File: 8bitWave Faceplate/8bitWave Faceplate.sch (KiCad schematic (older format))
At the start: 45 parts, among them IC1 0.96_I2C_OLED, J1 I2C_VOL, J2 SPI, J3 EXTENSION, M1 Mounting, M2 Mounting, M3 Mounting, M4 Mounting, U1 74HC595_ALT, U2 74HC595_ALT

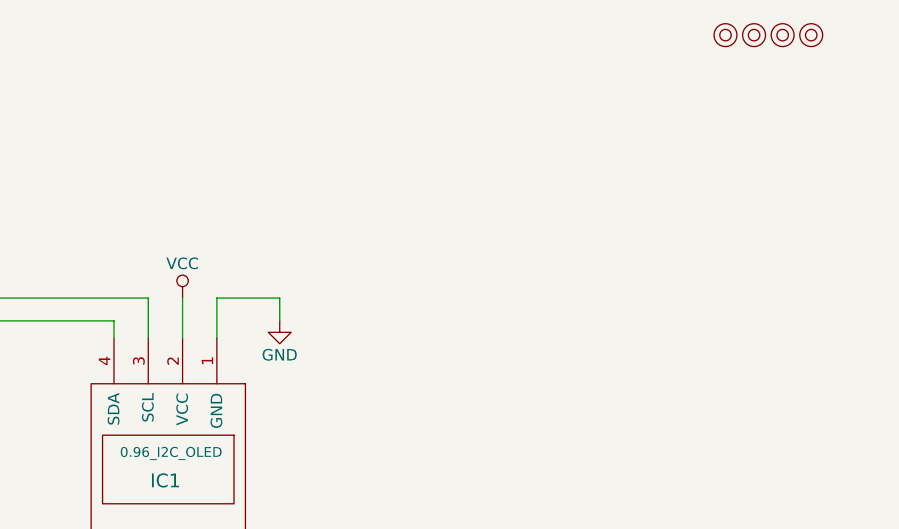
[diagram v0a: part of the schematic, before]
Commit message: Allow faceplate to choose OLED pin order
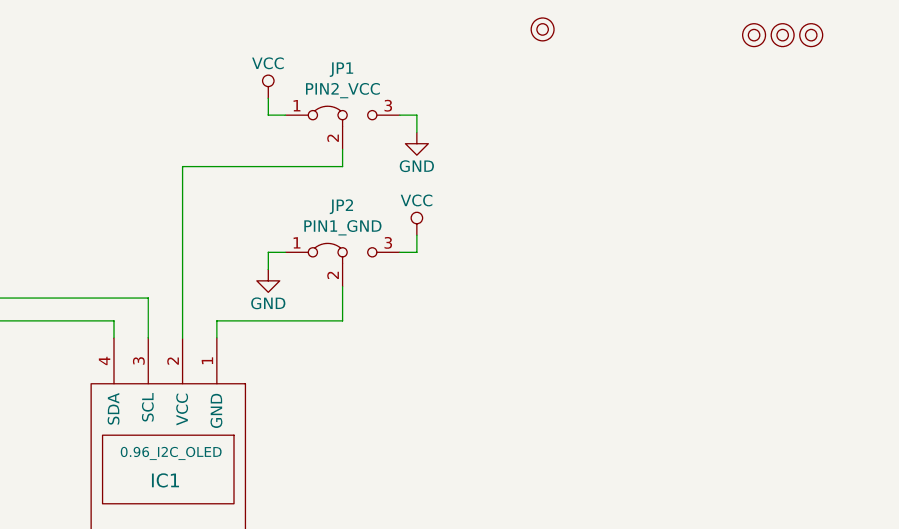
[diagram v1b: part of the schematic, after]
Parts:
- added JP1: PIN2_VCC, wire_pads:OLED_SEL, symbol Jumper:Jumper_3_Bridged12
- added JP2: PIN1_GND, wire_pads:OLED_SEL, symbol Jumper:Jumper_3_Bridged12
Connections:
- net GND: now also JP1.3 (B), JP2.1 (A); no longer IC1.1 (GND)
- net VCC: now also JP1.1 (A), JP2.3 (B); no longer IC1.2 (VCC)
- new net: IC1.1 (GND), JP2.2 (C)
- new net: IC1.2 (VCC), JP1.2 (C)
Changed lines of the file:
@@
 Title "8BIT WAVE Faceplate"
 Date ""
-Rev "A"
+Rev "B"
 Comp ""
 Comment1 ""
@@
 L mounting:Mounting M1
 U 1 1 5E3B603D
-P 10775 550
-F 0 "M1" H 10775 650 50  0001 C CNN
-F 1 "Mounting" H 10775 475 50  0001 C CNN
-F 2 "mounting:M3" H 10775 550 50  0001 C CNN
-F 3 "" H 10775 550 50  0001 C CNN
-	1    10775 550
+P 9975 525
+F 0 "M1" H 9975 625 50  0001 C CNN
+F 1 "Mounting" H 9975 450 50  0001 C CNN
+F 2 "mounting:M3" H 9975 525 50  0001 C CNN
+F 3 "" H 9975 525 50  0001 C CNN
+	1    9975 525
 	1    0    0    -1
 $EndComp
@@
 	7150 1900 7250 1800
 Wire Wire Line
-	8550 1700 8550 1875
-Wire Wire Line
 	8250 1700 7250 1700
 Wire Wire Line
@@
 Wire Wire Line
 	8100 1800 8100 1875
-Wire Wire Line
-	8550 1700 8825 1700
-Wire Wire Line
-	8825 1700 8825 1800
-$Comp
-L power:GND #PWR05
-U 1 1 5E3EF7B8
-P 8825 1800
-F 0 "#PWR05" H 8825 1550 50  0001 C CNN
-F 1 "GND" H 8825 1650 50  0000 C CNN
-F 2 "" H 8825 1800 50  0001 C CNN
-F 3 "" H 8825 1800 50  0001 C CNN
-	1    8825 1800
-	-1   0    0    -1
-$EndComp
-$Comp
-L power:VCC #PWR06
-U 1 1 5E3EF86D
-P 8400 1700
-F 0 "#PWR06" H 8400 1550 50  0001 C CNN
-F 1 "VCC" H 8400 1850 50  0000 C CNN
-F 2 "" H 8400 1700 50  0001 C CNN
-F 3 "" H 8400 1700 50  0001 C CNN
-	1    8400 1700
-	-1   0    0    -1
-$EndComp
-Wire Wire Line
-	8400 1700 8400 1875
 $Comp
 L power:GND #PWR07
@@
 NoConn ~ 1125 1575
 NoConn ~ 1125 1875
+Text Notes 1200 1625 0    60   ~ 0
+Not actually used at\nthis point, it is here\nas an option for\nmounting (and\nsymmetry).
+$Comp
+L Jumper:Jumper_3_Bridged12 JP2
+U 1 1 5ED85DD0
+P 9100 1500
+F 0 "JP2" H 9100 1704 50  0000 C CNN
+F 1 "PIN1_GND" H 9100 1613 50  0000 C CNN
+F 2 "wire_pads:OLED_SEL" H 9100 1500 50  0001 C CNN
+F 3 "~" H 9100 1500 50  0001 C CNN
+	1    9100 1500
+	1    0    0    -1
+$EndComp
+$Comp
+L Jumper:Jumper_3_Bridged12 JP1
+U 1 1 5ED8BDDA
+P 9100 900
+F 0 "JP1" H 9100 1104 50  0000 C CNN
+F 1 "PIN2_VCC" H 9100 1013 50  0000 C CNN
+F 2 "wire_pads:OLED_SEL" H 9100 900 50  0001 C CNN
+F 3 "~" H 9100 900 50  0001 C CNN
+	1    9100 900
+	1    0    0    -1
+$EndComp
+$Comp
+L power:GND #PWR0101
+U 1 1 5ED9181E
+P 8775 1575
+F 0 "#PWR0101" H 8775 1325 50  0001 C CNN
+F 1 "GND" H 8775 1425 50  0000 C CNN
+F 2 "" H 8775 1575 50  0001 C CNN
+F 3 "" H 8775 1575 50  0001 C CNN
+	1    8775 1575
+	-1   0    0    -1
+$EndComp
+Wire Wire Line
+	8775 1575 8775 1500
+Wire Wire Line
+	8775 1500 8850 1500
+Wire Wire Line
+	9350 1500 9425 1500
+Wire Wire Line
+	9425 1500 9425 1425
+$Comp
+L power:VCC #PWR0102
+U 1 1 5EDA6198
+P 9425 1425
+F 0 "#PWR0102" H 9425 1275 50  0001 C CNN
+F 1 "VCC" H 9425 1575 50  0000 C CNN
+F 2 "" H 9425 1425 50  0001 C CNN
+F 3 "" H 9425 1425 50  0001 C CNN
+	1    9425 1425
+	-1   0    0    -1
+$EndComp
+$Comp
+L power:VCC #PWR0103
+U 1 1 5EDABD2C
+P 8775 825
+F 0 "#PWR0103" H 8775 675 50  0001 C CNN
+F 1 "VCC" H 8775 975 50  0000 C CNN
+F 2 "" H 8775 825 50  0001 C CNN
+F 3 "" H 8775 825 50  0001 C CNN
+	1    8775 825
+	-1   0    0    -1
+$EndComp
+Wire Wire Line
+	8775 825  8775 900
+Wire Wire Line
+	8775 900  8850 900
+$Comp
+L power:GND #PWR0104
+U 1 1 5EDB6E50
+P 9425 975
+F 0 "#PWR0104" H 9425 725 50  0001 C CNN
+F 1 "GND" H 9425 825 50  0000 C CNN
+F 2 "" H 9425 975 50  0001 C CNN
+F 3 "" H 9425 975 50  0001 C CNN
+	1    9425 975
+	-1   0    0    -1
+$EndComp
+Wire Wire Line
+	9425 975  9425 900
+Wire Wire Line
+	9425 900  9350 900
+Wire Wire Line
+	9100 1800 8550 1800
+Wire Wire Line
+	8550 1875 8550 1800
+Wire Wire Line
+	9100 1050 9100 1125
+Wire Wire Line
+	9100 1125 8400 1125
+Wire Wire Line
+	9100 1650 9100 1800
+Wire Wire Line
+	8400 1125 8400 1875
 Wire Bus Line
 	5600 3925 5600 6150
 Wire Bus Line
 	5600 1675 5600 2075
-Text Notes 1200 1625 0    60   ~ 0
-Not actually used at\nthis point, it is here\nas an option for\nmounting (and\nsymmetry).
 $EndSCHEMATC
